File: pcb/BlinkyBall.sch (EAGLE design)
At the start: 18 parts, among them U1 Tiny85-20-SMT

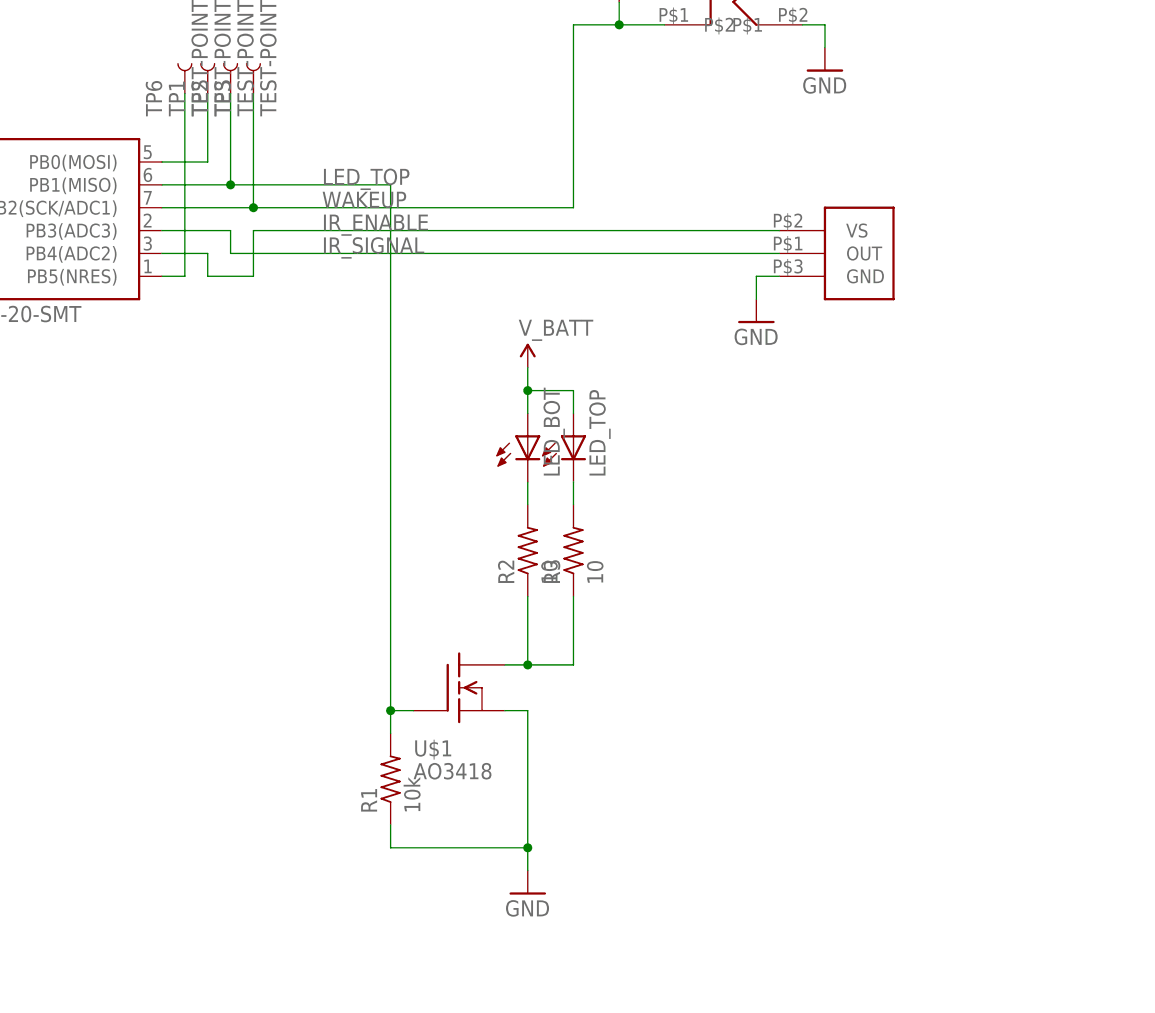
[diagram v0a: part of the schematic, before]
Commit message: RevC pcb design: rounded rect, switch IR pinout, space out test points
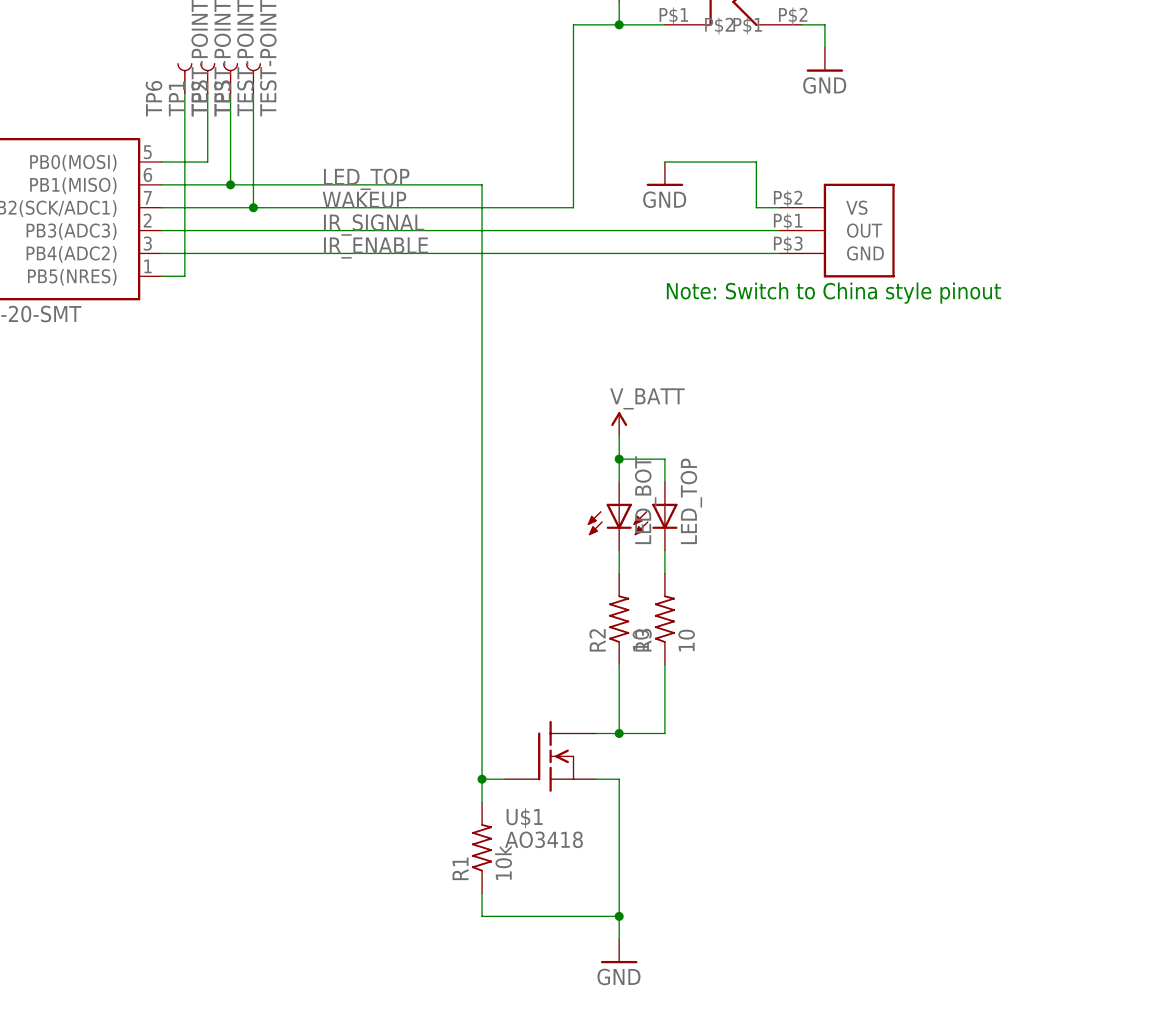
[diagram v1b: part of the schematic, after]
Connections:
- net GND: now also U$5.VS; no longer U$5.GND
- net IR_ENABLE: now also U$5.GND; no longer U$5.VS
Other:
- note added: "Note: Switch to China style pinout"
- moved on the sheet: LED_BOT, LED_TOP, R1, R2, R3, U$1
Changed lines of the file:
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@@
 <sheet>
 <plain>
+<text x="99.06" y="60.96" size="1.778" layer="91">Note: Switch to China style pinout</text>
 </plain>
 <instances>
@@
 <instance part="GND2" gate="1" x="7.62" y="50.8"/>
 <instance part="C1" gate="G$1" x="12.7" y="71.12"/>
-<instance part="U$5" gate="G$1" x="116.84" y="66.04"/>
-<instance part="R2" gate="G$1" x="83.82" y="33.02" rot="R90"/>
-<instance part="R3" gate="G$1" x="88.9" y="33.02" rot="R90"/>
+<instance part="U$5" gate="G$1" x="116.84" y="68.58"/>
+<instance part="R2" gate="G$1" x="93.98" y="25.4" rot="R90"/>
+<instance part="R3" gate="G$1" x="99.06" y="25.4" rot="R90"/>
 <instance part="R4" gate="G$1" x="93.98" y="99.06" rot="R90"/>
 <instance part="SUPPLY4" gate="G$1" x="93.98" y="106.68"/>
@@
 <instance part="TP5" gate="G$1" x="2.54" y="63.5" rot="R180"/>
 <instance part="TP6" gate="G$1" x="45.72" y="83.82" rot="R90"/>
-<instance part="LED_BOT" gate="G$1" x="83.82" y="45.72"/>
-<instance part="LED_TOP" gate="G$1" x="88.9" y="45.72"/>
-<instance part="GND5" gate="1" x="83.82" y="-5.08"/>
-<instance part="U$1" gate="G$1" x="73.66" y="17.78"/>
-<instance part="SUPPLY5" gate="G$1" x="83.82" y="53.34"/>
-<instance part="R1" gate="G$1" x="68.58" y="7.62" rot="R90"/>
-<instance part="GND4" gate="1" x="109.22" y="58.42"/>
+<instance part="LED_BOT" gate="G$1" x="93.98" y="38.1"/>
+<instance part="LED_TOP" gate="G$1" x="99.06" y="38.1"/>
+<instance part="GND5" gate="1" x="93.98" y="-12.7"/>
+<instance part="U$1" gate="G$1" x="83.82" y="10.16"/>
+<instance part="SUPPLY5" gate="G$1" x="93.98" y="45.72"/>
+<instance part="R1" gate="G$1" x="78.74" y="0" rot="R90"/>
+<instance part="GND4" gate="1" x="99.06" y="73.66"/>
 <instance part="U$3" gate="G$1" x="111.76" y="91.44"/>
 </instances>
@@
 <segment>
 <pinref part="LED_TOP" gate="G$1" pin="A"/>
-<wire x1="88.9" y1="48.26" x2="88.9" y2="50.8" width="0.1524" layer="91"/>
-<wire x1="88.9" y1="50.8" x2="83.82" y2="50.8" width="0.1524" layer="91"/>
+<wire x1="99.06" y1="40.64" x2="99.06" y2="43.18" width="0.1524" layer="91"/>
+<wire x1="99.06" y1="43.18" x2="93.98" y2="43.18" width="0.1524" layer="91"/>
 <pinref part="SUPPLY5" gate="G$1" pin="V_BATT"/>
-<wire x1="83.82" y1="50.8" x2="83.82" y2="53.34" width="0.1524" layer="91"/>
+<wire x1="93.98" y1="43.18" x2="93.98" y2="45.72" width="0.1524" layer="91"/>
 <pinref part="LED_BOT" gate="G$1" pin="A"/>
-<wire x1="83.82" y1="50.8" x2="83.82" y2="48.26" width="0.1524" layer="91"/>
-<junction x="83.82" y="50.8"/>
+<wire x1="93.98" y1="43.18" x2="93.98" y2="40.64" width="0.1524" layer="91"/>
+<junction x="93.98" y="43.18"/>
 </segment>
 </net>
@@
 </segment>
 <segment>
-<wire x1="81.28" y1="15.24" x2="83.82" y2="15.24" width="0.1524" layer="91"/>
+<wire x1="91.44" y1="7.62" x2="93.98" y2="7.62" width="0.1524" layer="91"/>
 <pinref part="GND5" gate="1" pin="GND"/>
-<wire x1="83.82" y1="15.24" x2="83.82" y2="0" width="0.1524" layer="91"/>
+<wire x1="93.98" y1="7.62" x2="93.98" y2="-7.62" width="0.1524" layer="91"/>
 <pinref part="U$1" gate="G$1" pin="S"/>
 <pinref part="R1" gate="G$1" pin="1"/>
-<wire x1="83.82" y1="0" x2="83.82" y2="-2.54" width="0.1524" layer="91"/>
-<wire x1="83.82" y1="0" x2="68.58" y2="0" width="0.1524" layer="91"/>
-<wire x1="68.58" y1="0" x2="68.58" y2="2.54" width="0.1524" layer="91"/>
-<junction x="83.82" y="0"/>
-</segment>
-<segment>
-<pinref part="U$5" gate="G$1" pin="GND"/>
-<wire x1="111.76" y1="63.5" x2="109.22" y2="63.5" width="0.1524" layer="91"/>
-<pinref part="GND4" gate="1" pin="GND"/>
-<wire x1="109.22" y1="63.5" x2="109.22" y2="60.96" width="0.1524" layer="91"/>
+<wire x1="93.98" y1="-7.62" x2="93.98" y2="-10.16" width="0.1524" layer="91"/>
+<wire x1="93.98" y1="-7.62" x2="78.74" y2="-7.62" width="0.1524" layer="91"/>
+<wire x1="78.74" y1="-7.62" x2="78.74" y2="-5.08" width="0.1524" layer="91"/>
+<junction x="93.98" y="-7.62"/>
 </segment>
 <segment>
@@
 <wire x1="114.3" y1="91.44" x2="116.84" y2="91.44" width="0.1524" layer="91"/>
 <wire x1="116.84" y1="91.44" x2="116.84" y2="88.9" width="0.1524" layer="91"/>
+</segment>
+<segment>
+<pinref part="U$5" gate="G$1" pin="VS"/>
+<pinref part="GND4" gate="1" pin="GND"/>
+<wire x1="111.76" y1="71.12" x2="109.22" y2="71.12" width="0.1524" layer="91"/>
+<wire x1="109.22" y1="71.12" x2="109.22" y2="76.2" width="0.1524" layer="91"/>
+<wire x1="109.22" y1="76.2" x2="99.06" y2="76.2" width="0.1524" layer="91"/>
 </segment>
 </net>
@@
 <pinref part="U1" gate="G$1" pin="PB1(MISO)"/>
 <wire x1="43.18" y1="73.66" x2="50.8" y2="73.66" width="0.1524" layer="91"/>
-<wire x1="50.8" y1="73.66" x2="68.58" y2="73.66" width="0.1524" layer="91"/>
+<wire x1="50.8" y1="73.66" x2="78.74" y2="73.66" width="0.1524" layer="91"/>
 <label x="60.96" y="73.66" size="1.778" layer="95"/>
 <pinref part="TP2" gate="G$1" pin="1"/>
 <wire x1="50.8" y1="83.82" x2="50.8" y2="73.66" width="0.1524" layer="91"/>
 <junction x="50.8" y="73.66"/>
-<wire x1="68.58" y1="73.66" x2="68.58" y2="15.24" width="0.1524" layer="91"/>
-<wire x1="71.12" y1="15.24" x2="68.58" y2="15.24" width="0.1524" layer="91"/>
+<wire x1="78.74" y1="73.66" x2="78.74" y2="7.62" width="0.1524" layer="91"/>
+<wire x1="81.28" y1="7.62" x2="78.74" y2="7.62" width="0.1524" layer="91"/>
 <pinref part="U$1" gate="G$1" pin="G"/>
 <pinref part="R1" gate="G$1" pin="2"/>
-<wire x1="68.58" y1="15.24" x2="68.58" y2="12.7" width="0.1524" layer="91"/>
-<junction x="68.58" y="15.24"/>
+<wire x1="78.74" y1="7.62" x2="78.74" y2="5.08" width="0.1524" layer="91"/>
+<junction x="78.74" y="7.62"/>
 </segment>
 </net>
@@
 <net name="IR_ENABLE" class="0">
 <segment>
-<pinref part="U$5" gate="G$1" pin="VS"/>
-<wire x1="111.76" y1="68.58" x2="53.34" y2="68.58" width="0.1524" layer="91"/>
+<label x="60.96" y="66.04" size="1.778" layer="95"/>
+<wire x1="111.76" y1="66.04" x2="43.18" y2="66.04" width="0.1524" layer="91"/>
+<pinref part="U1" gate="G$1" pin="PB4(ADC2)"/>
+<pinref part="U$5" gate="G$1" pin="GND"/>
+</segment>
+</net>
+<net name="IR_SIGNAL" class="0">
+<segment>
 <label x="60.96" y="68.58" size="1.778" layer="95"/>
-<wire x1="53.34" y1="68.58" x2="53.34" y2="63.5" width="0.1524" layer="91"/>
-<wire x1="53.34" y1="63.5" x2="48.26" y2="63.5" width="0.1524" layer="91"/>
-<wire x1="48.26" y1="63.5" x2="48.26" y2="66.04" width="0.1524" layer="91"/>
-<pinref part="U1" gate="G$1" pin="PB4(ADC2)"/>
-<wire x1="48.26" y1="66.04" x2="43.18" y2="66.04" width="0.1524" layer="91"/>
-</segment>
-</net>
-<net name="IR_SIGNAL" class="0">
-<segment>
+<pinref part="U1" gate="G$1" pin="PB3(ADC3)"/>
+<wire x1="43.18" y1="68.58" x2="111.76" y2="68.58" width="0.1524" layer="91"/>
 <pinref part="U$5" gate="G$1" pin="OUT"/>
-<wire x1="111.76" y1="66.04" x2="50.8" y2="66.04" width="0.1524" layer="91"/>
-<label x="60.96" y="66.04" size="1.778" layer="95"/>
-<pinref part="U1" gate="G$1" pin="PB3(ADC3)"/>
-<wire x1="43.18" y1="68.58" x2="50.8" y2="68.58" width="0.1524" layer="91"/>
-<wire x1="50.8" y1="68.58" x2="50.8" y2="66.04" width="0.1524" layer="91"/>
 </segment>
 </net>
@@
 <pinref part="LED_BOT" gate="G$1" pin="C"/>
 <pinref part="R2" gate="G$1" pin="2"/>
-<wire x1="83.82" y1="40.64" x2="83.82" y2="38.1" width="0.1524" layer="91"/>
+<wire x1="93.98" y1="33.02" x2="93.98" y2="30.48" width="0.1524" layer="91"/>
 </segment>
 </net>
@@
 <pinref part="LED_TOP" gate="G$1" pin="C"/>
 <pinref part="R3" gate="G$1" pin="2"/>
-<wire x1="88.9" y1="40.64" x2="88.9" y2="38.1" width="0.1524" layer="91"/>
+<wire x1="99.06" y1="33.02" x2="99.06" y2="30.48" width="0.1524" layer="91"/>
 </segment>
 </net>
@@
 <segment>
 <pinref part="R2" gate="G$1" pin="1"/>
-<wire x1="83.82" y1="27.94" x2="83.82" y2="20.32" width="0.1524" layer="91"/>
+<wire x1="93.98" y1="20.32" x2="93.98" y2="12.7" width="0.1524" layer="91"/>
 <pinref part="U$1" gate="G$1" pin="D"/>
-<wire x1="83.82" y1="20.32" x2="81.28" y2="20.32" width="0.1524" layer="91"/>
+<wire x1="93.98" y1="12.7" x2="91.44" y2="12.7" width="0.1524" layer="91"/>
 <pinref part="R3" gate="G$1" pin="1"/>
-<wire x1="88.9" y1="27.94" x2="88.9" y2="20.32" width="0.1524" layer="91"/>
-<wire x1="88.9" y1="20.32" x2="83.82" y2="20.32" width="0.1524" layer="91"/>
-<junction x="83.82" y="20.32"/>
+<wire x1="99.06" y1="20.32" x2="99.06" y2="12.7" width="0.1524" layer="91"/>
+<wire x1="99.06" y1="12.7" x2="93.98" y2="12.7" width="0.1524" layer="91"/>
+<junction x="93.98" y="12.7"/>
 </segment>
 </net>
@@
 </sheet>
 </sheets>
+<errors>
+</errors>
 </schematic>
 </drawing>

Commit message: More design tweaks
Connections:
- net GND: now also U$3.P$1; no longer U$3.P$2
- net WAKEUP: now also U$3.P$2; no longer U$3.P$1
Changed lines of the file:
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@@
 <instance part="R1" gate="G$1" x="78.74" y="0" rot="R90"/>
 <instance part="GND4" gate="1" x="99.06" y="73.66"/>
-<instance part="U$3" gate="G$1" x="111.76" y="91.44"/>
+<instance part="U$3" gate="G$1" x="99.06" y="91.44" rot="MR0"/>
 </instances>
 <busses>
@@
 </segment>
 <segment>
-<pinref part="U$3" gate="G$1" pin="P$2"/>
 <pinref part="GND3" gate="1" pin="GND"/>
-<wire x1="114.3" y1="91.44" x2="116.84" y2="91.44" width="0.1524" layer="91"/>
 <wire x1="116.84" y1="91.44" x2="116.84" y2="88.9" width="0.1524" layer="91"/>
+<pinref part="U$3" gate="G$1" pin="P$1"/>
+<wire x1="111.76" y1="91.44" x2="116.84" y2="91.44" width="0.1524" layer="91"/>
 </segment>
 <segment>
@@
 <wire x1="53.34" y1="83.82" x2="53.34" y2="71.12" width="0.1524" layer="91"/>
 <junction x="53.34" y="71.12"/>
-<pinref part="U$3" gate="G$1" pin="P$1"/>
-<wire x1="99.06" y1="91.44" x2="93.98" y2="91.44" width="0.1524" layer="91"/>
+<pinref part="U$3" gate="G$1" pin="P$2"/>
+<wire x1="96.52" y1="91.44" x2="93.98" y2="91.44" width="0.1524" layer="91"/>
 <junction x="93.98" y="91.44"/>
 </segment>
